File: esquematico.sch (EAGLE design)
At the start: 30 parts, among them IC1 TS321IDBVR, IC2 ESP32-S3-WROOM-1-N16R8, IC3 MAX30102EFD+T, K1 G6RW, M1 ELECTRET_MICROPHON-WM.64PN, U1 LP38692SD-3.3/NOPB, U2 MCP73831T-2ACI/OT, U4 USB4115-03-C

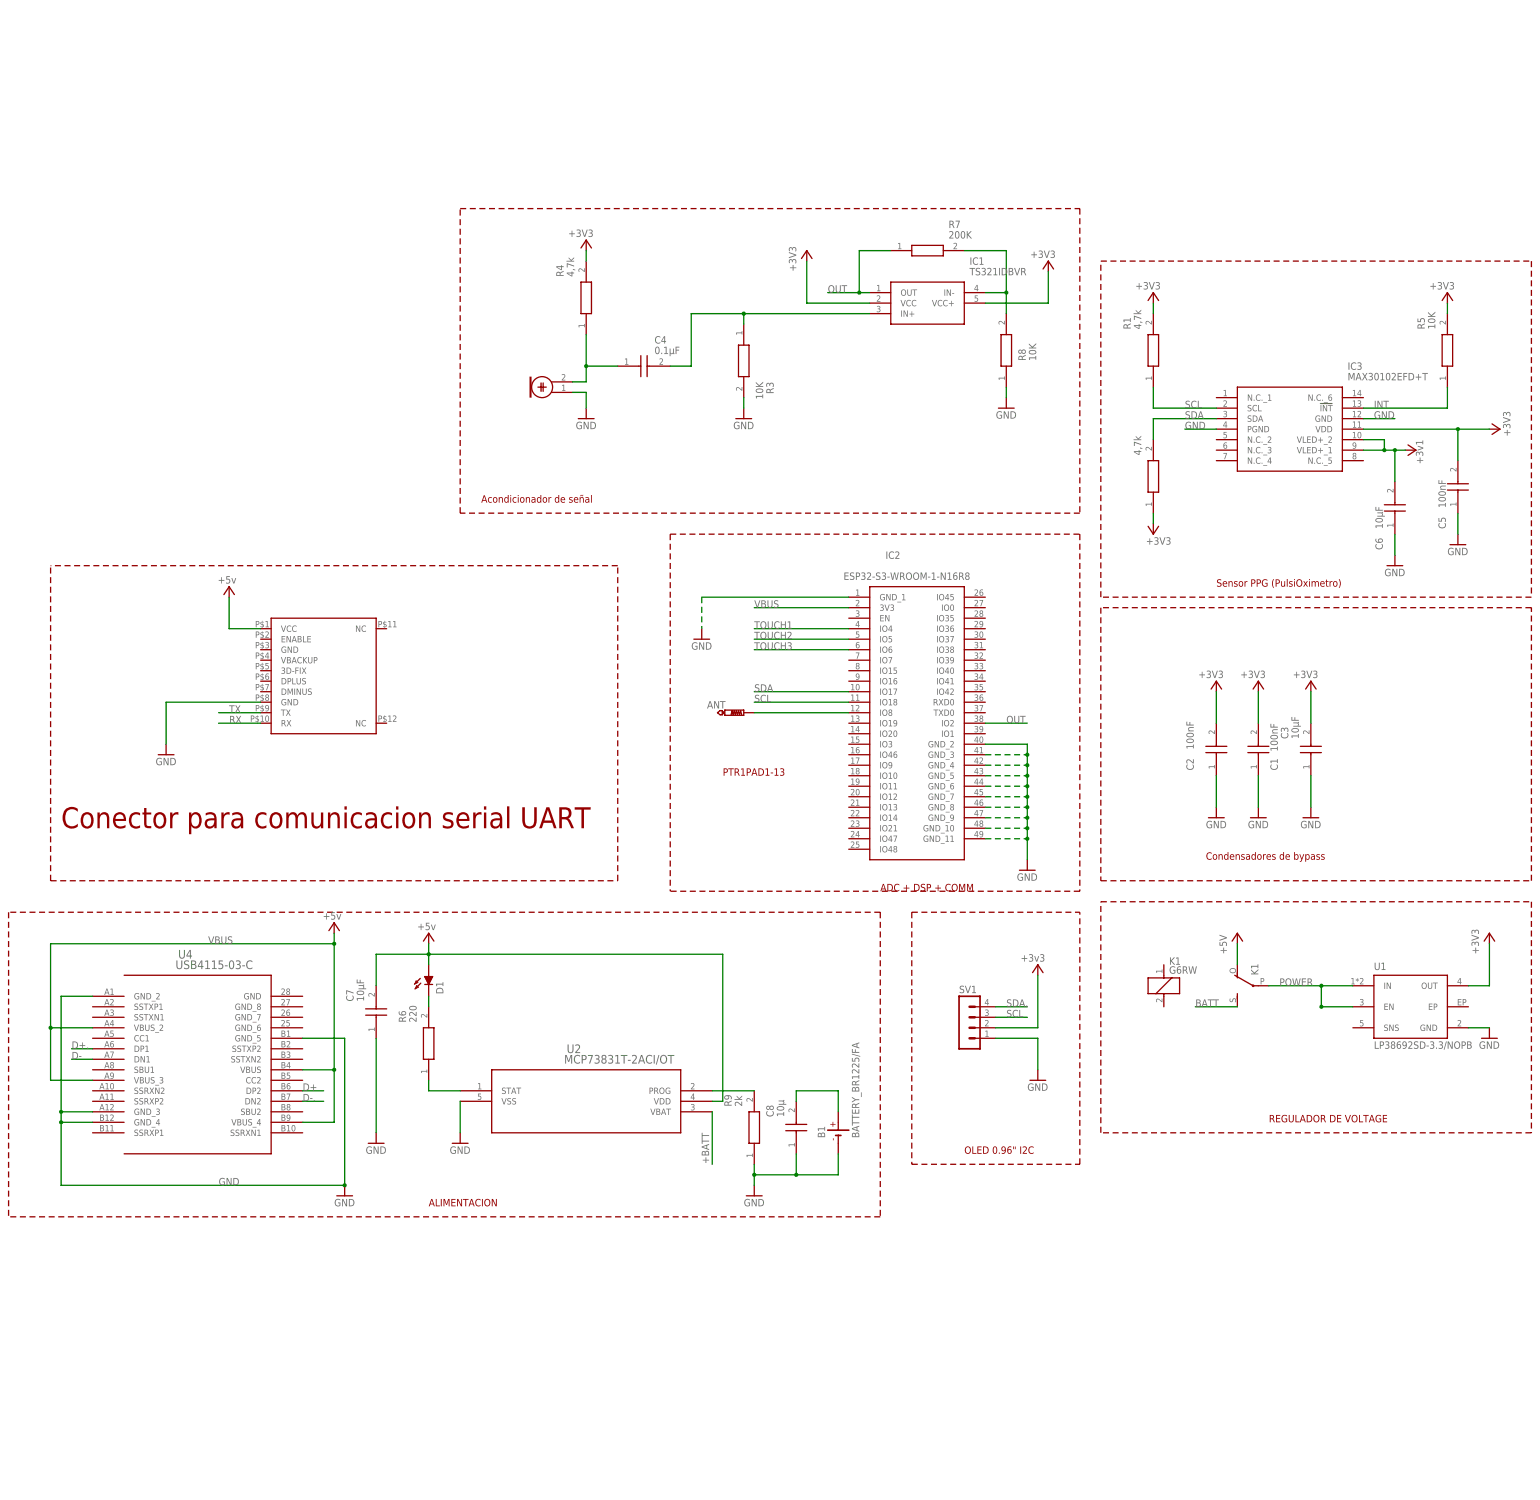
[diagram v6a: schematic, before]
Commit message: se cambio nombre al esquematico.s## a .sch
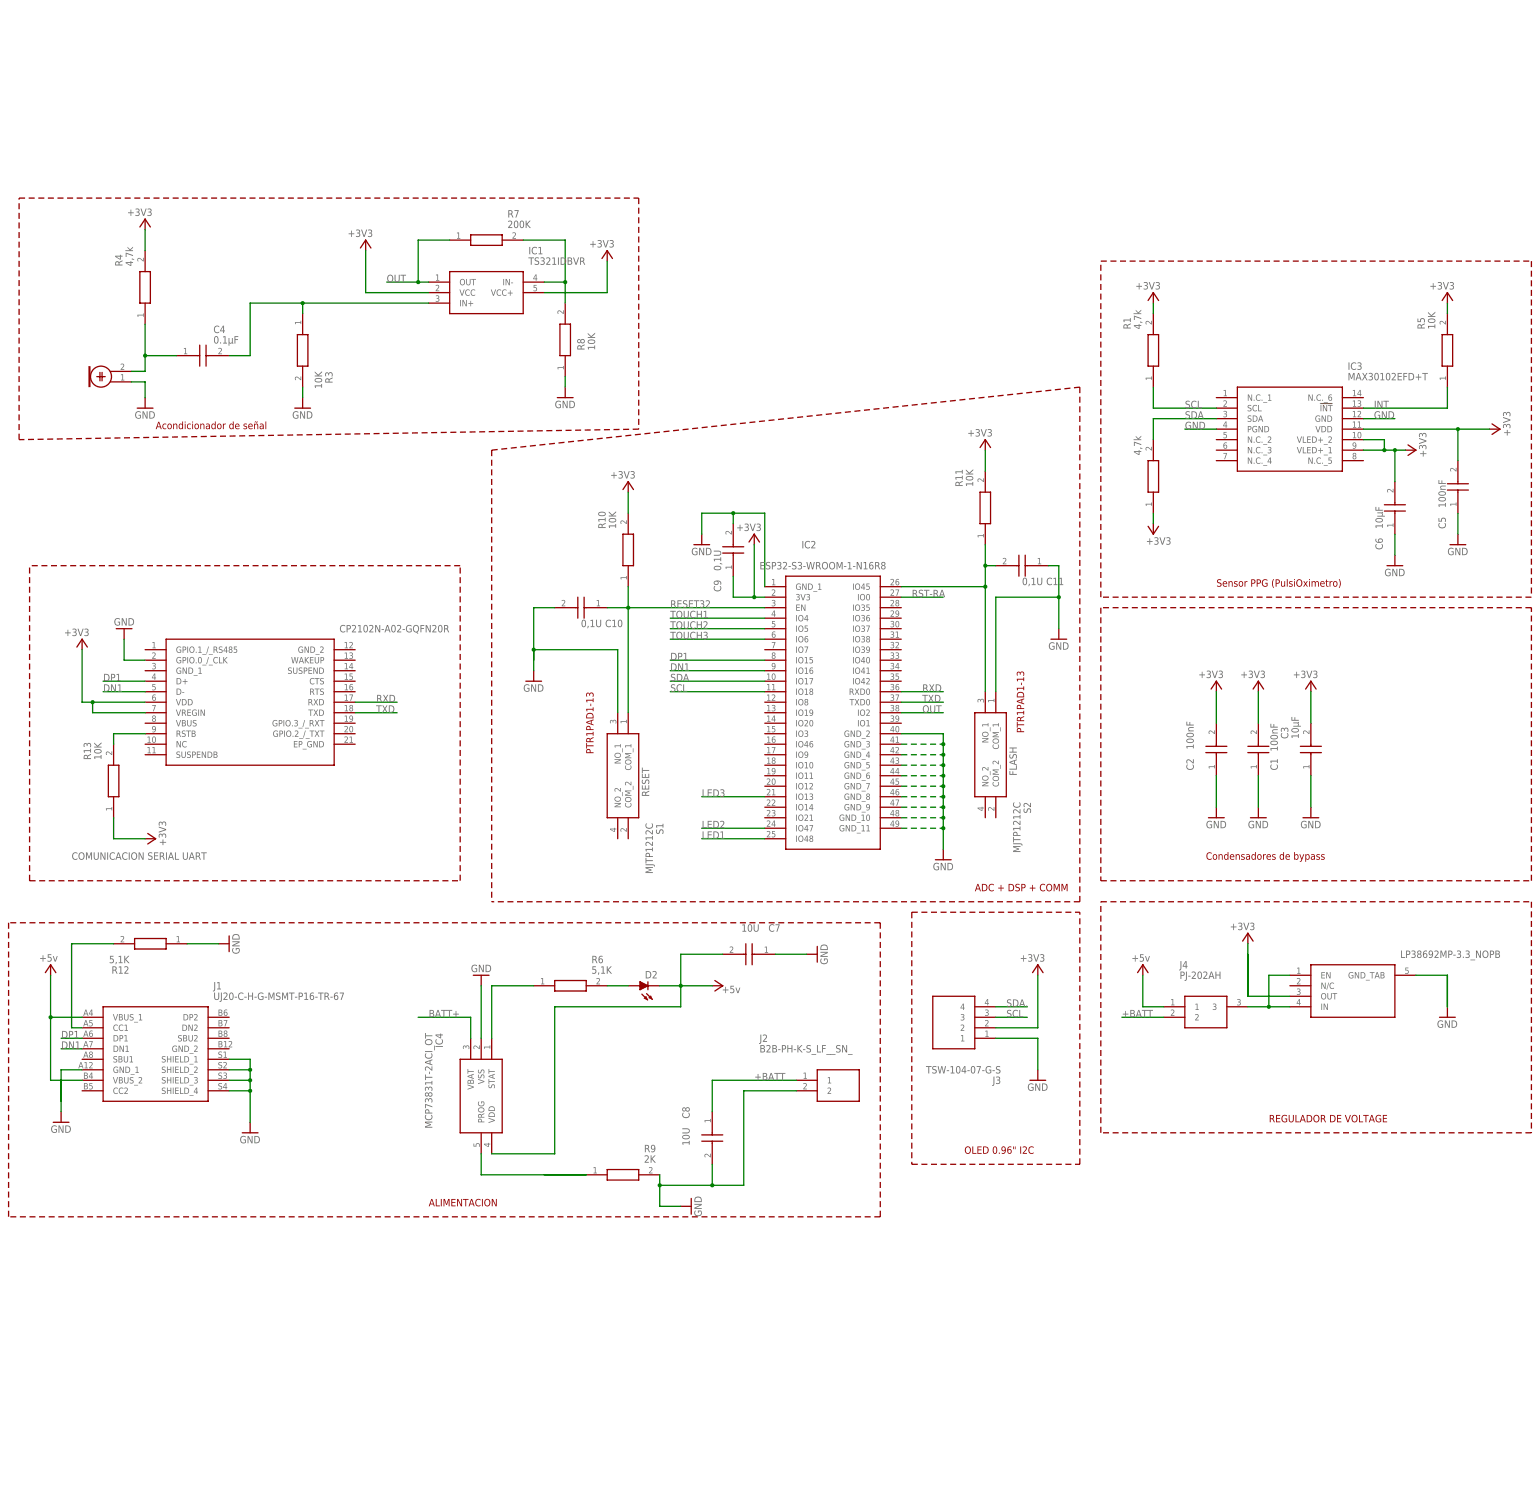
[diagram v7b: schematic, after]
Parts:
- removed ANT: PTR1PAD1-13, testpad:PTR1PAD1-13
- removed B1: BATTERY_BR1225/FA, 52101-101-REV-A_v16:BATTERY_BR1225/FA
- removed D1: (no value), 52101-101-REV-A_v16:LED_LEDCHIP-LED0603MP
- removed K1: G6RW, relay:G6RW
- removed SV1: (no value), con-lstb:MA04-1
- removed U1: LP38692SD-3.3/NOPB, LDO:LP38692SD-3.3/NOPB
- removed U2: MCP73831T-2ACI/OT, MCP73831:MCP73831T-2ACI/OT
- removed U3: (no value), adafruit:GPS_FGPMMOPA6B
- removed U4: USB4115-03-C, usb:USB4115-03-C
- added C10, C11, C9: 0,1U, C0805J104K1RACAUTO:C0805J104K1RACAUTO
- added D2: (no value), 52101-101-REV-A_v16:LED_LEDCHIP-LED0603MP
- added IC4: MCP73831T-2ACI_OT, MCP73831T-2ACI_OT:MCP73831T-2ACI_OT
- added IC5: LP38692MP-3.3_NOPB, LP38692MP-3.3_NOPB:LP38692MP-3.3_NOPB
- added IC6: CP2102N-A02-GQFN20R, CP2102N-A02-GQFN20R:CP2102N-A02-GQFN20R
- added J1: UJ20-C-H-G-MSMT-P16-TR-67, UJ20-C-H-G-MSMT-P16-TR-67:UJ20-C-H-G-MSMT-P16-TR-67
- added J2: B2B-PH-K-S_LF__SN_, B2B-PH-K-S_LF__SN_:B2B-PH-K-S_LF__SN_
- added J3: TSW-104-07-G-S, TSW-104-07-G-S:TSW-104-07-G-S
- added J4: PJ-202AH, PJ-202AH:PJ-202AH
- added R10, R11, R13: 10K, 0805S8F1202P5E:0805S8F1202P5E
- added R12: 5,1K, 0805S8F1202P5E:0805S8F1202P5E
- added S1, S2: MJTP1212C, MJTP1212C:MJTP1212C
- C7: value 10µF -> 10U
- C8: value 10µ -> 10U
- R6: value 220 -> 5,1K
- R9: value 2k -> 2K
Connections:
- removed net ANT: ANT.TP, IC2.IO8
- removed net BATT: K12.S
- removed net D+: U4.DP2
- removed net D+.: U4.DP1
- removed net D-: U4.DN1
- removed net D-.: U4.DN2
- removed net N$7: B1.+, C8.2
- removed net N$9: SV1.2
- removed net POWER: K12.P, U1.EN, U1.IN
- removed net RX: U3.RX
- removed net TX: U3.TX
- new net +3V3: C1.2, C3.2, C5.2, C6.2, C9.1, IC1.VCC, IC1.VCC+, IC2.3V3, IC3.VDD, IC3.VLED+_1, IC3.VLED+_2, IC6.VDD, IC6.VREGIN, J1.VBUS_1, J1.VBUS_2, J3.2, J4.1, R1.2, R10.2, R11.2, R13.1, R2.1, R4.2, R5.2
- new net BATT+: IC4.VBAT
- new net DN1: IC2.IO16, IC6.D-, J1.DN1
- new net DP1: IC2.IO15, IC6.D+, J1.DP1
- new net GND1: C11.2, IC2.IO45, R11.1, S2.NO_1
- new net GND3: C8.1, J2.1
- new net INT1: R10.1
- new net LED1: IC2.IO48
- new net LED2: IC2.IO47
- new net LED3: IC2.IO13
- new net N$10: J1.GND_1
- new net N$11: IC5.OUT
- new net N$12: C7.2, D2.C, IC4.VDD
- new net N$13: IC4.PROG, R9.1
- new net N$14: IC5.GND_TAB
- new net N$15: IC6.RSTB, R13.2
- new net N$8: J1.CC1, R12.2
- new net RESET32: C10.1, IC2.EN, S1.COM_1
- new net RST-RA: IC2.IO0
- new net RXD: IC2.RXD0, IC6.RXD
- new net TXD: IC2.TXD0, IC6.TXD
- net +BATT: now also J4.2; no longer U2.VBAT
- net GND: now also C10.2, C11.1, C8.2, C9.2, IC4.VSS, IC6.GPIO.0_/_CLK, J1.SHIELD_1, J1.SHIELD_2, J1.SHIELD_3, J1.SHIELD_4, J2.2, J3.1, R12.1, R9.2, S1.NO_1, S2.COM_1; no longer B1.-, C8.1, R9.1, SV1.1, U1.GND, U2.VSS, U3.GND@2, U4.GND_2, U4.GND_3, U4.GND_4, U4.GND_5
- net N$3: now also IC4.STAT, R6.1; no longer D1.C, R6.2
- net N$5: now also D2.A, R6.2; no longer R6.1, U2.STAT
- net N$6: now also IC5.EN, IC5.IN, J4.3; no longer R9.2, U2.PROG
- net SCL: now also J3.3; no longer SV1.3
- net SDA.: now also J3.4; no longer SV1.4
- net VBUS: no longer C1.2, C3.2, C5.2, C6.2, C7.2, D1.A, IC1.VCC, IC1.VCC+, IC2.3V3, IC3.VDD, IC3.VLED+_1, IC3.VLED+_2, K12.O, R1.2, R2.1, R4.2, R5.2, U1.OUT, U2.VDD, U3.VCC, U4.VBUS, U4.VBUS_2, U4.VBUS_3, U4.VBUS_4
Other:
- note added: "+BATT"
- note added: "COMUNICACION SERIAL UART"
- note added: "FLASH"
- note added: "RESET"
- note removed: "Conector para comunicacion serial UART"
- moved on the sheet: C4, C7, C8, IC1, IC2, R3, R4, R6, R7, R8, R9

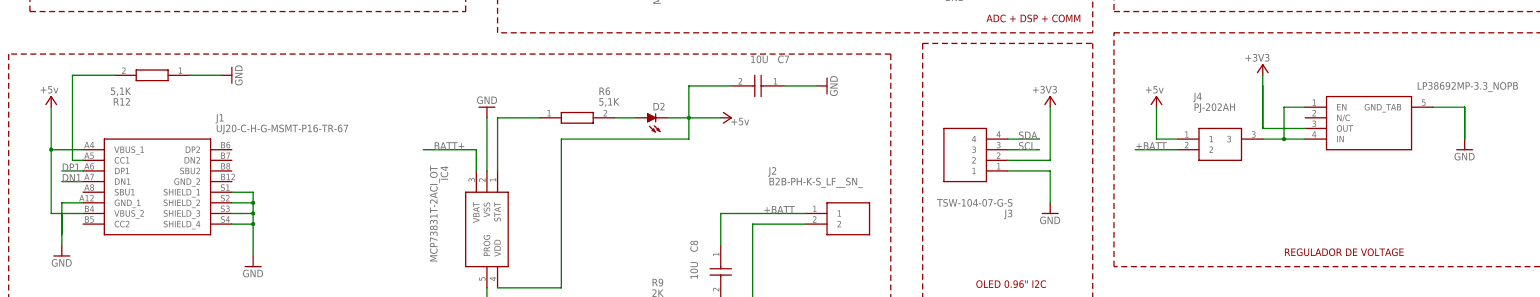
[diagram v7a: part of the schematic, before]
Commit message: se agrego el pcb de ejemplo
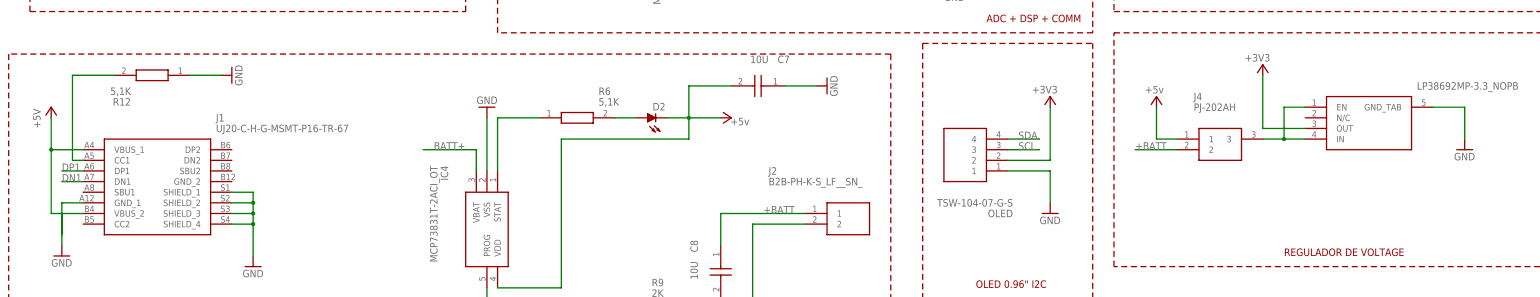
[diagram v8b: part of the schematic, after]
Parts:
- renumbered J3 to OLED
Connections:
- removed net N$11: IC5.OUT
- removed net N$14: IC5.GND_TAB
- new net +5V: J1.VBUS_1, J1.VBUS_2
- net +3V3: now also IC5.OUT; no longer J1.VBUS_1, J1.VBUS_2
- net GND: now also IC5.GND_TAB
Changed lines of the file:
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@@
 <part name="M1" library="microphon" library_urn="urn:adsk.eagle:library:297" deviceset="ELECTRET_MICROPHON-" device="WM.64PN" package3d_urn="urn:adsk.eagle:package:21039/1"/>
 <part name="GND14" library="supply1" library_urn="urn:adsk.eagle:library:371" deviceset="GND" device=""/>
-<part name="+3V13" library="supply1" library_urn="urn:adsk.eagle:library:371" deviceset="+3V3" device="" value="+5v"/>
 <part name="S1" library="MJTP1212C" deviceset="MJTP1212C" device=""/>
 <part name="R10" library="0805S8F1202P5E" deviceset="0805S8F1202P5E" device="" value="10K"/>
@@
 <part name="J2" library="B2B-PH-K-S_LF__SN_" deviceset="B2B-PH-K-S_LF__SN_" device=""/>
 <part name="C8" library="C0805J104K1RACAUTO" deviceset="C0805J104K1RACAUTO" device="" value="10U"/>
-<part name="J3" library="TSW-104-07-G-S" deviceset="TSW-104-07-G-S" device=""/>
+<part name="OLED" library="TSW-104-07-G-S" deviceset="TSW-104-07-G-S" device=""/>
 <part name="IC5" library="LP38692MP-3.3_NOPB" deviceset="LP38692MP-3.3_NOPB" device=""/>
 <part name="J4" library="PJ-202AH" deviceset="PJ-202AH" device=""/>
@@
 <part name="+3V4" library="supply1" library_urn="urn:adsk.eagle:library:371" deviceset="+3V3" device=""/>
 <part name="+3V15" library="supply1" library_urn="urn:adsk.eagle:library:371" deviceset="+3V3" device=""/>
+<part name="P+1" library="supply1" library_urn="urn:adsk.eagle:library:371" deviceset="+5V" device=""/>
 </parts>
 <sheets>
@@
 <attribute name="VALUE" x="251.46" y="38.1" size="1.778" layer="96"/>
 </instance>
-<instance part="+3V13" gate="G$1" x="15.24" y="68.58" smashed="yes">
-<attribute name="VALUE" x="17.018" y="71.12" size="1.778" layer="96" rot="R180"/>
-</instance>
 <instance part="S1" gate="G$1" x="154.94" y="129.54" smashed="yes" rot="R270">
 <attribute name="NAME" x="162.56" y="102.87" size="1.778" layer="95" rot="R270" align="center-left"/>
@@
 <attribute name="VALUE" x="168.91" y="29.21" size="1.778" layer="96" rot="R270" align="center-left"/>
 </instance>
-<instance part="J3" gate="G$1" x="243.84" y="50.8" smashed="yes" rot="R180">
+<instance part="OLED" gate="G$1" x="243.84" y="50.8" smashed="yes" rot="R180">
 <attribute name="NAME" x="245.11" y="40.64" size="1.778" layer="95" rot="R180" align="center-left"/>
 <attribute name="VALUE" x="245.11" y="43.18" size="1.778" layer="96" rot="R180" align="center-left"/>
@@
 <instance part="+3V15" gate="G$1" x="304.8" y="76.2" smashed="yes">
 <attribute name="VALUE" x="306.578" y="78.74" size="1.778" layer="96" rot="R180"/>
+</instance>
+<instance part="P+1" gate="1" x="15.24" y="66.04" smashed="yes">
+<attribute name="VALUE" x="12.7" y="60.96" size="1.778" layer="96" rot="R90"/>
 </instance>
 </instances>
@@
 <segment>
 <label x="246.38" y="55.88" size="1.778" layer="95"/>
-<pinref part="J3" gate="G$1" pin="3"/>
+<pinref part="OLED" gate="G$1" pin="3"/>
 <wire x1="243.84" y1="55.88" x2="251.46" y2="55.88" width="0.1524" layer="91"/>
 </segment>
@@
 <wire x1="243.84" y1="50.8" x2="254" y2="50.8" width="0.1524" layer="91"/>
 <wire x1="254" y1="50.8" x2="254" y2="43.18" width="0.1524" layer="91"/>
-<pinref part="J3" gate="G$1" pin="1"/>
+<pinref part="OLED" gate="G$1" pin="1"/>
 </segment>
 <segment>
@@
 <pinref part="GND13" gate="1" pin="GND"/>
 </segment>
+<segment>
+<pinref part="IC5" gate="G$1" pin="GND_TAB"/>
+<pinref part="GND11" gate="1" pin="GND"/>
+<wire x1="345.44" y1="66.04" x2="353.06" y2="66.04" width="0.1524" layer="91"/>
+<wire x1="353.06" y1="66.04" x2="353.06" y2="58.42" width="0.1524" layer="91"/>
+</segment>
 </net>
 <net name="INT" class="0">
@@
 <segment>
 <label x="246.38" y="58.42" size="1.778" layer="95"/>
-<pinref part="J3" gate="G$1" pin="4"/>
+<pinref part="OLED" gate="G$1" pin="4"/>
 <wire x1="243.84" y1="58.42" x2="251.46" y2="58.42" width="0.1524" layer="91"/>
 </segment>
@@
 <net name="+3V3" class="0">
 <segment>
-<pinref part="J1" gate="G$1" pin="VBUS_2"/>
-<wire x1="22.86" y1="40.64" x2="15.24" y2="40.64" width="0.1524" layer="91"/>
-<wire x1="15.24" y1="40.64" x2="15.24" y2="55.88" width="0.1524" layer="91"/>
-<pinref part="J1" gate="G$1" pin="VBUS_1"/>
-<wire x1="15.24" y1="66.04" x2="15.24" y2="55.88" width="0.1524" layer="91"/>
-<wire x1="15.24" y1="55.88" x2="22.86" y2="55.88" width="0.1524" layer="91"/>
-<junction x="15.24" y="55.88"/>
-<pinref part="+3V13" gate="G$1" pin="+3V3"/>
-</segment>
-<segment>
 <pinref part="J4" gate="G$1" pin="1"/>
 <wire x1="284.48" y1="58.42" x2="279.4" y2="58.42" width="0.1524" layer="91"/>
@@
 <wire x1="243.84" y1="53.34" x2="254" y2="53.34" width="0.1524" layer="91"/>
 <wire x1="254" y1="53.34" x2="254" y2="66.04" width="0.1524" layer="91"/>
-<pinref part="J3" gate="G$1" pin="2"/>
+<pinref part="OLED" gate="G$1" pin="2"/>
 <pinref part="+3V16" gate="G$1" pin="+3V3"/>
 </segment>
@@
 </segment>
 <segment>
-<wire x1="304.8" y1="60.96" x2="304.8" y2="73.66" width="0.1524" layer="91"/>
 <pinref part="+3V15" gate="G$1" pin="+3V3"/>
+<pinref part="IC5" gate="G$1" pin="OUT"/>
+<wire x1="304.8" y1="73.66" x2="304.8" y2="60.96" width="0.1524" layer="91"/>
+<wire x1="304.8" y1="60.96" x2="314.96" y2="60.96" width="0.1524" layer="91"/>
 </segment>
 </net>
@@
 </segment>
 </net>
-<net name="N$11" class="0">
-<segment>
-<pinref part="IC5" gate="G$1" pin="OUT"/>
-<wire x1="314.96" y1="60.96" x2="304.8" y2="60.96" width="0.1524" layer="91"/>
-<wire x1="304.8" y1="60.96" x2="304.8" y2="71.12" width="0.1524" layer="91"/>
-</segment>
-</net>
-<net name="N$14" class="0">
-<segment>
-<pinref part="IC5" gate="G$1" pin="GND_TAB"/>
-<wire x1="345.44" y1="66.04" x2="353.06" y2="66.04" width="0.1524" layer="91"/>
-<wire x1="353.06" y1="66.04" x2="353.06" y2="58.42" width="0.1524" layer="91"/>
-<pinref part="GND11" gate="1" pin="GND"/>
-<wire x1="353.06" y1="66.04" x2="353.06" y2="58.42" width="0.1524" layer="91"/>
-</segment>
-</net>
 <net name="RXD" class="0">
 <segment>
@@
 </segment>
 </net>
+<net name="+5V" class="0">
+<segment>
+<pinref part="J1" gate="G$1" pin="VBUS_2"/>
+<wire x1="22.86" y1="40.64" x2="15.24" y2="40.64" width="0.1524" layer="91"/>
+<wire x1="15.24" y1="40.64" x2="15.24" y2="55.88" width="0.1524" layer="91"/>
+<pinref part="J1" gate="G$1" pin="VBUS_1"/>
+<wire x1="15.24" y1="55.88" x2="22.86" y2="55.88" width="0.1524" layer="91"/>
+<pinref part="P+1" gate="1" pin="+5V"/>
+<wire x1="15.24" y1="63.5" x2="15.24" y2="55.88" width="0.1524" layer="91"/>
+<junction x="15.24" y="55.88"/>
+</segment>
+</net>
